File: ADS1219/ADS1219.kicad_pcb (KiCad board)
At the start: 2 copper layers, 25 x 25 mm, 28 parts, among them J1 qwiic, J2 Conn_01x06, J3 qwiic, J4 DRDY, U1 ADS1219IPW, U2 NCP51460SN33T1G

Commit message: Adding vref and drdy
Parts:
- removed TP1, TP2, TP3, TP4, TP5, TP6, TP7, TP8, TP9: TestPoint, TestPoint:TestPoint_Pad_1.0x1.0mm
- moved U2 0.50 mm to (173.5, 92.0), turned to 180 degrees
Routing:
- net /AIN1: track 32.7 -> 12.2 mm
- net /AIN0: track 25.4 -> 13.9 mm
- net /SDA: track 49.2 -> 42.7 mm
- net /A1: track 17.4 -> 12.1 mm, vias 1 -> 0
- net /AIN3: track 16.1 -> 12.1 mm
- net /AIN2: track 12.8 -> 10.2 mm
- net Net-(U1-Pad9): track 4.16 -> 2.58 mm
- net /SCL: track 35.5 -> 34.3 mm
- net +3.3V: track 70.3 -> 69.1 mm
- net GND: vias 9 -> 6

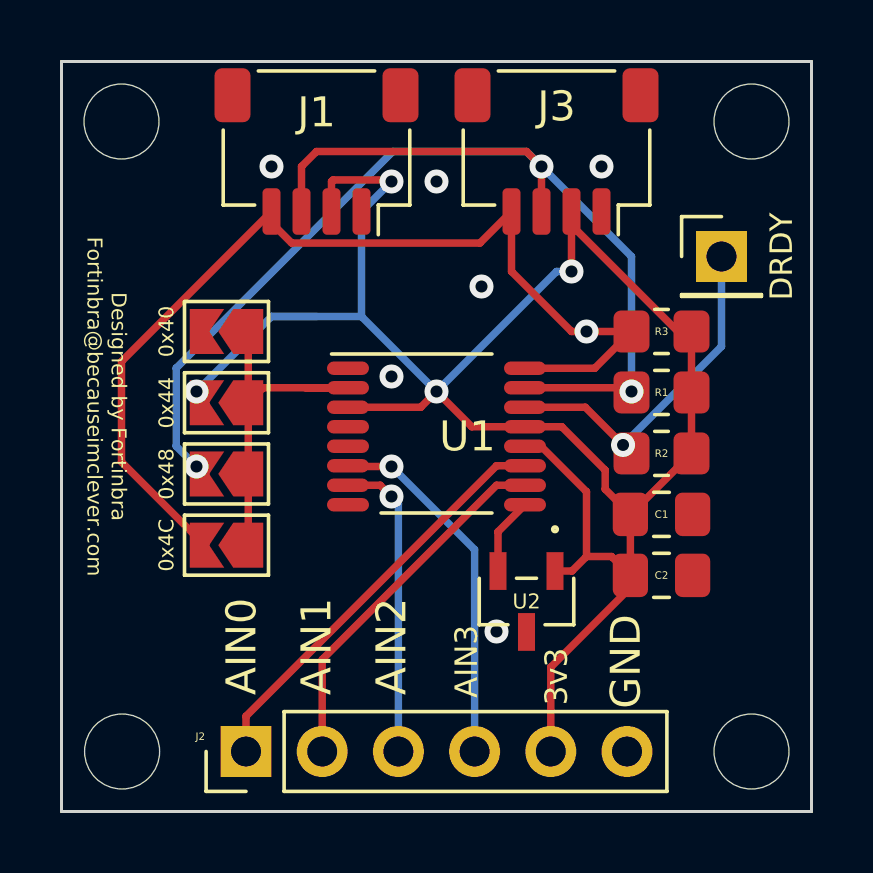
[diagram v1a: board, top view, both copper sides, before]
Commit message: Updating to KiCad 7
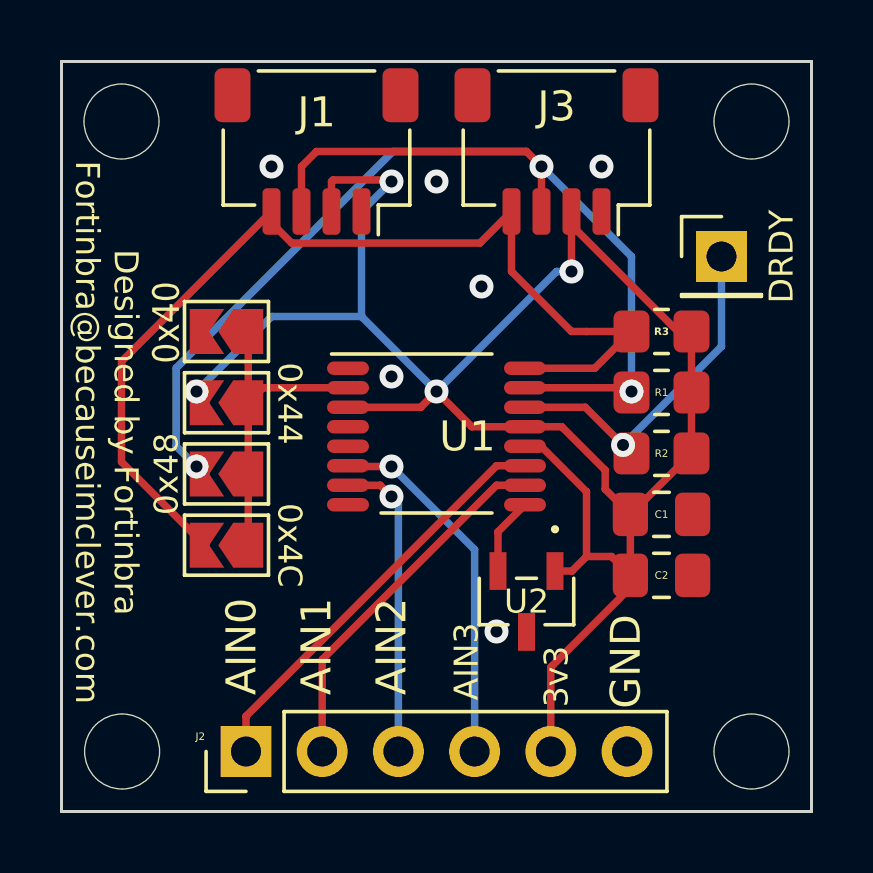
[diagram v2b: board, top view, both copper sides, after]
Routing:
- net +3.3V: track 69.1 -> 67.6 mm
- net /A1: track 12.1 -> 10.7 mm
- net /SCL: vias 1 -> 0
